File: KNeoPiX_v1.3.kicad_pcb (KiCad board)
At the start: 4 copper layers, 24.5 x 34.6 mm, 35 parts, among them J1 Conn_KNX, J2 Conn_KNX, J3 Screw Terminal - Non Isolated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, J4 Screw Terminal - Isolated IOs, J5 Conn_01x05, J6 Conn_01x05, SW1 Prog BTN, U1 Seeeduino XIAO, U2 LM2937IMP-3.3 / 5.0, U3 ADuM1201AR / ADum1250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

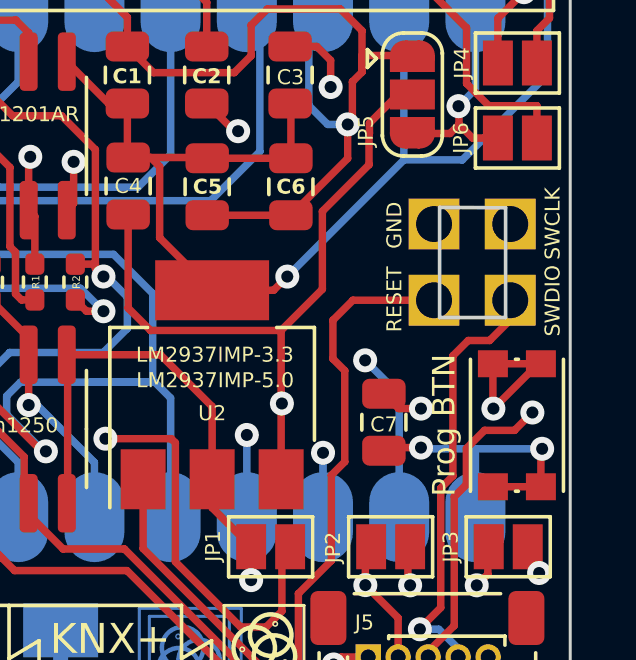
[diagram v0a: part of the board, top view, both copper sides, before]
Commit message: Changed the pcb cut-out to customized wholes
Since a clean cutout costs more. Therefore, lets try with this one.
Btw. This is also the same cut out on PicoKNeoPix.
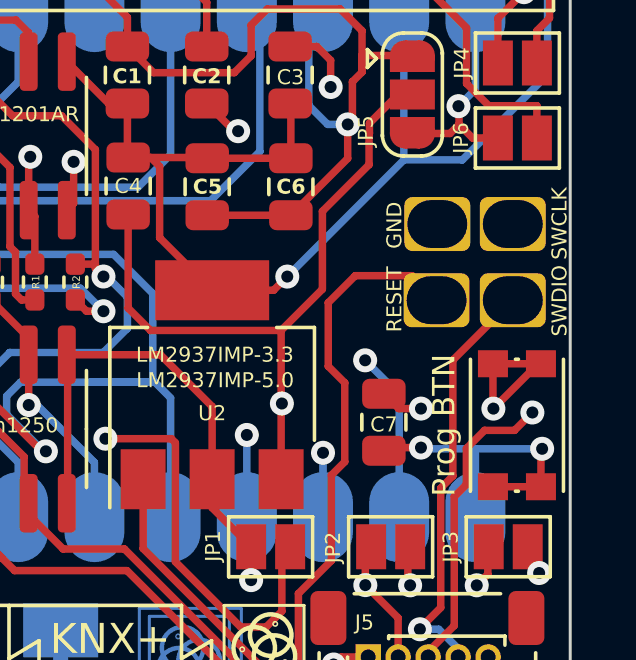
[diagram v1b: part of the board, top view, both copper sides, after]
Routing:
- net RESET: track 25.4 -> 26.7 mm
- net EXT_GND: track 110.2 -> 111.2 mm
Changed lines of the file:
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@@
   (paper "A4")
   (title_block
-    (comment 4 "PCBWay Project ID: 0a7519d4-7a83-4fb8-a160-ce3eb0eff894")
+    (title "KNeoPix")
+    (date "2023-02-25")
+    (rev "1.3")
+    (company "OpenKNX")
   )
   (layers
@@
         (effects (font (size 0.5 0.5) (thickness 0.125)))
     )
-    (fp_text user "SWDIO" (at 7.7987 20.8583 90 unlocked) (layer "F.SilkS")
+    (fp_text user "SWDIO" (at 7.7987 21.0883 90 unlocked) (layer "F.SilkS")
         (effects (font (size 0.5 0.5) (thickness 0.125)))
     )
-    (fp_text user "SWCLK" (at 10.3737 20.8583 90 unlocked) (layer "F.SilkS")
+    (fp_text user "SWCLK" (at 10.3737 21.0883 90 unlocked) (layer "F.SilkS")
         (effects (font (size 0.5 0.5) (thickness 0.125)))
     )
@@
       )
       (stroke (width 0.0254) (type solid)) (fill none) (layer "B.SilkS"))
-    (fp_line (start 7.24 17.09) (end 7.24 19.29)
-      (stroke (width 0.12) (type default)) (layer "Edge.Cuts"))
-    (fp_line (start 7.24 17.09) (end 10.91 17.09)
-      (stroke (width 0.12) (type default)) (layer "Edge.Cuts"))
-    (fp_line (start 10.9 19.29) (end 7.24 19.29)
-      (stroke (width 0.12) (type default)) (layer "Edge.Cuts"))
-    (fp_line (start 10.91 17.09) (end 10.9 19.29)
-      (stroke (width 0.12) (type default)) (layer "Edge.Cuts"))
     (fp_line (start 0.185786 19.12762) (end 0.185786 2.191663)
       (stroke (width 0.0254) (type solid)) (layer "B.Fab"))
@@
     (pad "14" smd oval (at 17.585786 18.284214 90) (size 3 2) (layers "B.Cu" "B.Paste" "B.Mask")
       (net 22 "5V-MCU") (pinfunction "5V") (pintype "unspecified"))
-    (pad "17" thru_hole rect (at 7.815786 19.444954 90) (size 1.7 1.7) (drill 1.2) (layers "*.Cu" "*.Mask")
+    (pad "17" thru_hole roundrect (at 7.815786 19.53 270) (size 1.8 2.2) (drill oval 1.6 2) (layers "*.Cu" "*.Mask") (roundrect_rratio 0.15)
       (net 27 "SWDIO") (pinfunction "PA31_SWDIO") (pintype "input"))
-    (pad "18" thru_hole rect (at 10.355786 19.444954 90) (size 1.7 1.7) (drill 1.2) (layers "*.Cu" "*.Mask")
+    (pad "18" thru_hole roundrect (at 10.355786 19.53 270) (size 1.8 2.2) (drill oval 1.6 2) (layers "*.Cu" "*.Mask") (roundrect_rratio 0.15)
       (net 26 "SWCLK") (pinfunction "PA30_SWCLK") (pintype "input"))
-    (pad "19" thru_hole rect (at 7.815786 16.904954 90) (size 1.7 1.7) (drill 1.2) (layers "*.Cu" "*.Mask")
+    (pad "19" thru_hole roundrect (at 7.815786 16.99 270) (size 1.8 2.2) (drill oval 1.6 2) (layers "*.Cu" "*.Mask") (roundrect_rratio 0.15)
       (net 28 "RESET") (pinfunction "RESET") (pintype "input"))
-    (pad "20" thru_hole rect (at 10.355786 16.904954 90) (size 1.7 1.7) (drill 1.2) (layers "*.Cu" "*.Mask")
+    (pad "20" thru_hole roundrect (at 10.355786 17.015046 270) (size 1.8 2.2) (drill oval 1.6 2) (layers "*.Cu" "*.Mask") (roundrect_rratio 0.15)
       (net 19 "EXT_GND") (pinfunction "GND") (pintype "input"))
     (model "${KIPRJMOD}/KNeoPix.3D-Models/Seeeduino XIAO SAMD21 v4.step" hide
@@
   (segment (start 131.4104 114.17) (end 129.045 114.17) (width 0.25) (layer "In1.Cu") (net 19))
   (segment (start 126.9549 112.0799) (end 126.9549 109.7692) (width 0.25) (layer "In1.Cu") (net 19))
+  (segment (start 131.158832 107.22) (end 129.36 107.22) (width 0.25) (layer "In1.Cu") (net 19))
   (segment (start 129.045 114.17) (end 126.9549 112.0799) (width 0.25) (layer "In1.Cu") (net 19))
   (segment (start 128.5 122.6995) (end 128.5 125.261) (width 0.25) (layer "In1.Cu") (net 19))
-  (segment (start 126.9549 109.5851) (end 128.52 108.02) (width 0.25) (layer "In1.Cu") (net 19))
-  (segment (start 128.52 108.02) (end 131.80236 108.02) (width 0.25) (layer "In1.Cu") (net 19))
+  (segment (start 131.956746 108.017914) (end 131.158832 107.22) (width 0.25) (layer "In1.Cu") (net 19))
+  (segment (start 126.9549 109.6251) (end 126.9549 109.7692) (width 0.25) (layer "In1.Cu") (net 19))
+  (segment (start 129.36 107.22) (end 126.9549 109.6251) (width 0.25) (layer "In1.Cu") (net 19))
   (segment (start 132.522 125.753) (end 128.992 125.753) (width 0.25) (layer "In1.Cu") (net 19))
   (segment (start 128.5 125.261) (end 128.992 125.753) (width 0.25) (layer "In1.Cu") (net 19))
@@
   (segment (start 135.125 114.3) (end 134.53 114.895) (width 0.25) (layer "F.Cu") (net 26))
   (via (at 135.125 114.3) (size 0.8) (drill 0.4) (layers "F.Cu" "B.Cu") (net 26))
-  (segment (start 135.5705 108.2455) (end 135.342914 108.017914) (width 0.25) (layer "In1.Cu") (net 26))
-  (segment (start 135.5705 113.8545) (end 135.5705 108.2455) (width 0.25) (layer "In1.Cu") (net 26))
-  (segment (start 135.342914 108.017914) (end 134.386654 108.017914) (width 0.25) (layer "In1.Cu") (net 26))
-  (segment (start 135.125 114.3) (end 135.5705 113.8545) (width 0.25) (layer "In1.Cu") (net 26))
-  (segment (start 132.475 116.415) (end 132.475 112.41) (width 0.25) (layer "F.Cu") (net 27))
-  (segment (start 131.375 121.5) (end 132.07 120.805) (width 0.25) (layer "F.Cu") (net 27))
+  (segment (start 135.8967 113.5283) (end 135.125 114.3) (width 0.25) (layer "In1.Cu") (net 26))
+  (segment (start 134.4717 108.017914) (end 135.8967 109.442914) (width 0.25) (layer "In1.Cu") (net 26))
+  (segment (start 135.8967 109.442914) (end 135.8967 113.5283) (width 0.25) (layer "In1.Cu") (net 26))
+  (segment (start 132.475 116.415) (end 132.475 112.554614) (width 0.25) (layer "F.Cu") (net 27))
   (segment (start 132.07 116.82) (end 132.475 116.415) (width 0.25) (layer "F.Cu") (net 27))
-  (segment (start 132.985 111.9) (end 133.7 111.9) (width 0.25) (layer "F.Cu") (net 27))
-  (segment (start 132.65 122.45) (end 132.65 123.65) (width 0.25) (layer "F.Cu") (net 27))
-  (segment (start 133.7 111.9) (end 134.394331 111.205669) (width 0.25) (layer "F.Cu") (net 27))
   (segment (start 131.375 121.525) (end 131.375 121.5) (width 0.25) (layer "F.Cu") (net 27))
+  (segment (start 132.65 122.45) (end 132.65 123.65) (width 0.25) (layer "F.Cu") (net 27))
+  (segment (start 131.375 121.5) (end 132.07 120.805) (width 0.25) (layer "F.Cu") (net 27))
   (segment (start 132.07 120.805) (end 132.07 116.82) (width 0.25) (layer "F.Cu") (net 27))
-  (segment (start 132.475 112.41) (end 132.985 111.9) (width 0.25) (layer "F.Cu") (net 27))
+  (segment (start 134.4717 110.557914) (end 132.475 112.554614) (width 0.25) (layer "F.Cu") (net 27))
   (via (at 131.375 121.525) (size 0.8) (drill 0.4) (layers "F.Cu" "B.Cu") (net 27))
   (segment (start 131.375 121.525) (end 132.005 121.525) (width 0.25) (layer "B.Cu") (net 27))
@@
   (segment (start 128.8709 115.943105) (end 128.425 116.389005) (width 0.25) (layer "F.Cu") (net 28))
   (segment (start 133.625 123.675) (end 133.625 124.525) (width 0.25) (layer "F.Cu") (net 28))
-  (segment (start 128.8709 112.906305) (end 128.8709 115.943105) (width 0.25) (layer "F.Cu") (net 28))
   (segment (start 133.625 124.525) (end 133.375 124.775) (width 0.25) (layer "F.Cu") (net 28))
+  (segment (start 128.8709 113.3109) (end 128.32 112.76) (width 0.25) (layer "F.Cu") (net 28))
+  (segment (start 131.113786 109.74) (end 131.9317 110.557914) (width 0.25) (layer "F.Cu") (net 28))
   (segment (start 128.425 119.236827) (end 127.325 120.336827) (width 0.25) (layer "F.Cu") (net 28))
-  (segment (start 128.475 111.225) (end 128.475 112.510405) (width 0.25) (layer "F.Cu") (net 28))
-  (segment (start 129.142086 110.557914) (end 128.475 111.225) (width 0.25) (layer "F.Cu") (net 28))
   (segment (start 127.325 122.975805) (end 129.124195 124.775) (width 0.25) (layer "F.Cu") (net 28))
   (segment (start 133.375 124.775) (end 129.124195 124.775) (width 0.25) (layer "F.Cu") (net 28))
+  (segment (start 128.32 112.76) (end 128.32 110.64) (width 0.25) (layer "F.Cu") (net 28))
+  (segment (start 128.8709 115.943105) (end 128.8709 113.3109) (width 0.25) (layer "F.Cu") (net 28))
   (segment (start 128.425 116.389005) (end 128.425 119.236827) (width 0.25) (layer "F.Cu") (net 28))
-  (segment (start 131.806977 110.557914) (end 129.142086 110.557914) (width 0.25) (layer "F.Cu") (net 28))
+  (segment (start 128.32 110.64) (end 129.22 109.74) (width 0.25) (layer "F.Cu") (net 28))
   (segment (start 133.625 123.675) (end 133.625 122.475) (width 0.25) (layer "F.Cu") (net 28))
+  (segment (start 129.22 109.74) (end 131.113786 109.74) (width 0.25) (layer "F.Cu") (net 28))
   (segment (start 127.325 120.336827) (end 127.325 122.975805) (width 0.25) (layer "F.Cu") (net 28))
-  (segment (start 128.475 112.510405) (end 128.8709 112.906305) (width 0.25) (layer "F.Cu") (net 28))
   (group "" (id 02afdab7-1f58-49ba-9ecb-7063497064bc)
     (members
